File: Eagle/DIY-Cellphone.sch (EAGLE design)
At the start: 67 parts, among them IC1 MEGA1284, J1 ISP, U1 MCP73831, X1 BU-SMA-V, X3 CCM03-3002 R102

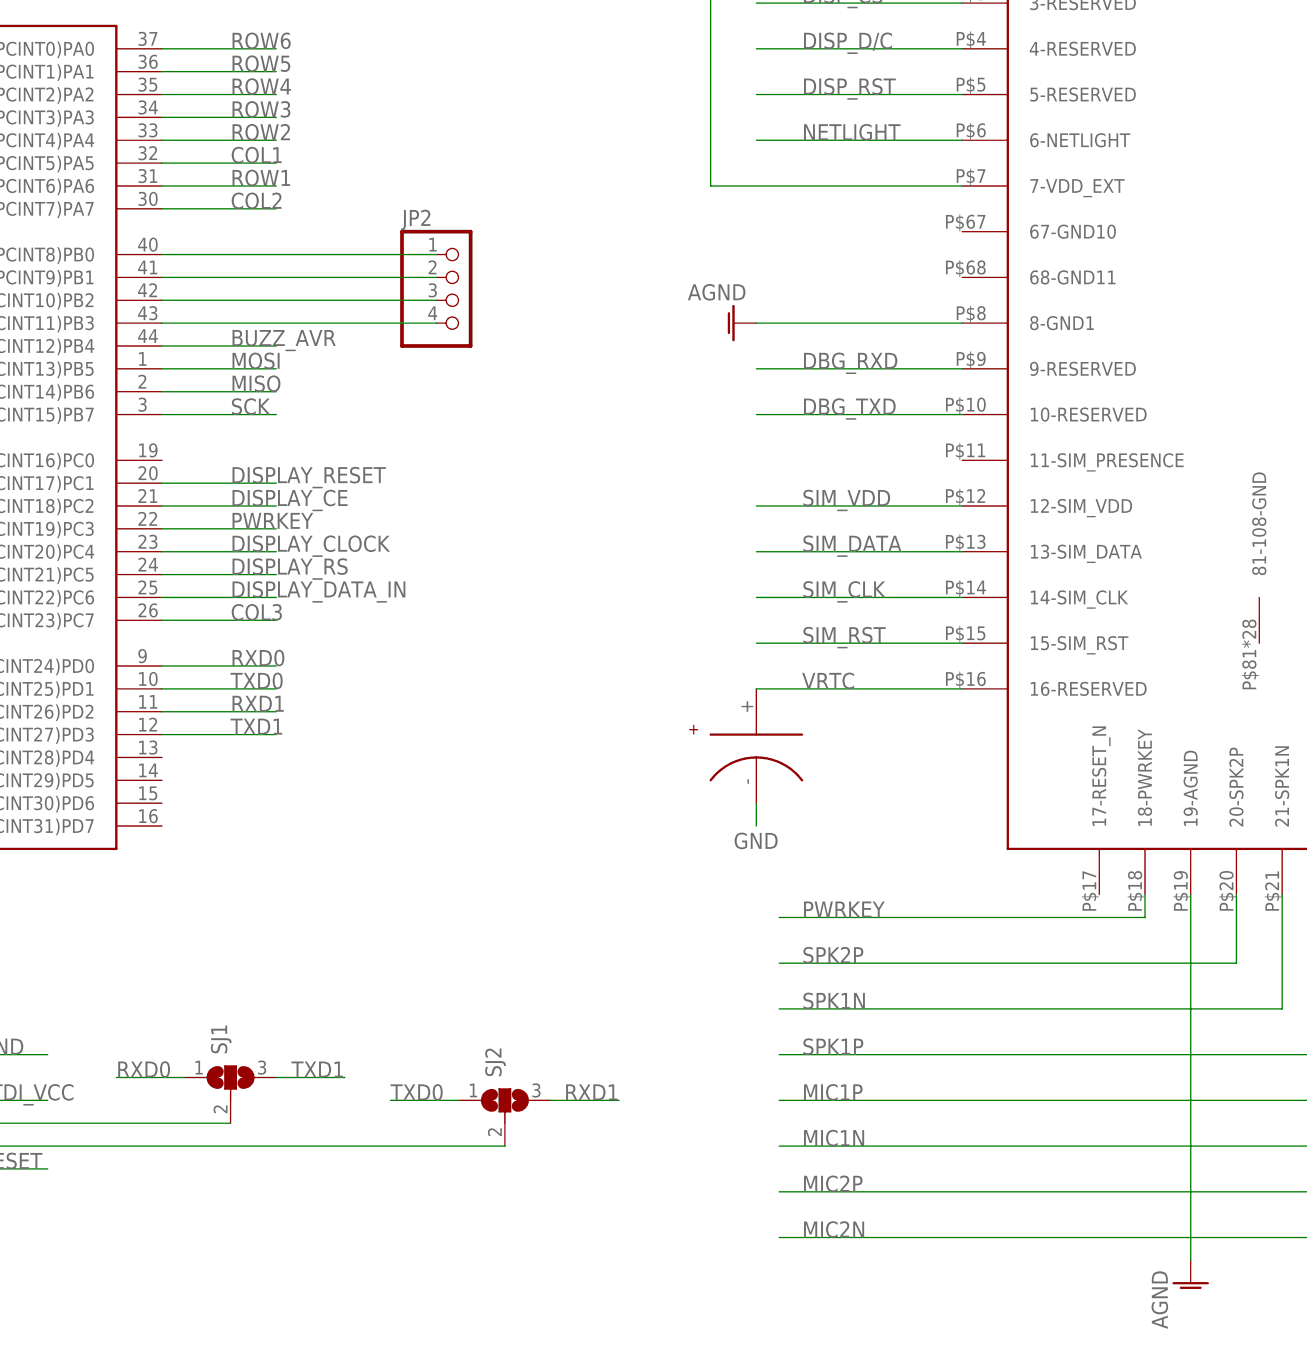
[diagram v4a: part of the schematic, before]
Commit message: Add transistors and finish routing.
PWRKEY and RESET_N now have transistors between UC15 module and
ATmega1284.
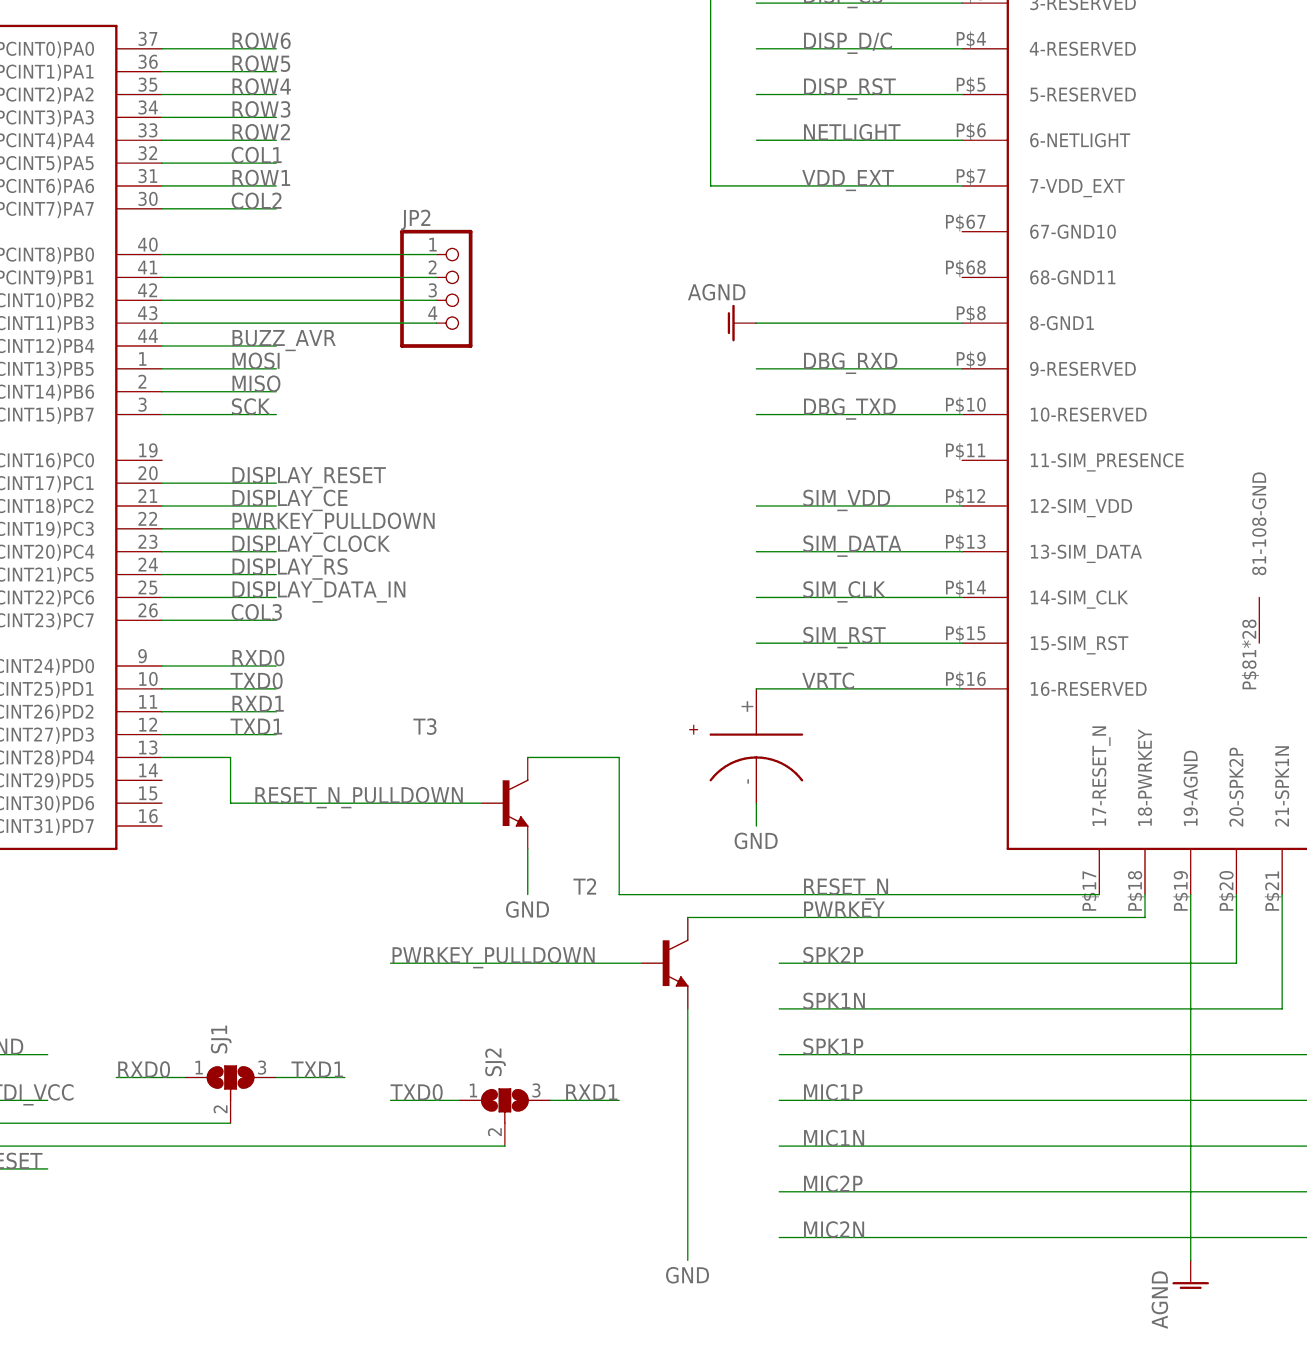
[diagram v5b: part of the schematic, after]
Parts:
- added T2, T3: (no value), transistor:MMBT3904LT1-NPN-SOT23-BEC
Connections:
- net N$2 renamed VDD_EXT
- new net PWRKEY_PULLDOWN: IC1.(TMS/PCINT19)PC3, T2.B
- new net RESET_N: T3.C, U$6.17-RESET_N
- new net RESET_N_PULLDOWN: IC1.(XCK1/OC1B/PCINT28)PD4, T3.B
- net GND: now also T2.E, T3.E
- net PWRKEY: now also T2.C; no longer IC1.(TMS/PCINT19)PC3
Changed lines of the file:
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@@
 <?xml version="1.0" encoding="utf-8"?>
 <!DOCTYPE eagle SYSTEM "eagle.dtd">
-<eagle version="6.6.0">
+<eagle version="7.1.0">
 <drawing>
 <settings>
@@
 <part name="U$6" library="cellphone" deviceset="UC15" device=""/>
 <part name="U2" library="SparkFun-DigitalIC" deviceset="TXB0104PWR" device="SOIC14"/>
+<part name="T2" library="transistor" deviceset="*-NPN-" device="SOT23-BEC" technology="MMBT3904LT1"/>
+<part name="T3" library="transistor" deviceset="*-NPN-" device="SOT23-BEC" technology="MMBT3904LT1"/>
 </parts>
 <sheets>
@@
 <instance part="U$6" gate="G$1" x="147.32" y="91.44"/>
 <instance part="U2" gate="G$1" x="76.2" y="172.72" rot="R180"/>
+<instance part="T2" gate="G$1" x="60.96" y="7.62"/>
+<instance part="T3" gate="G$1" x="43.18" y="25.4"/>
 </instances>
 <busses>
@@
 <label x="73.66" y="200.66" size="1.778" layer="95"/>
 </segment>
+<segment>
+<pinref part="T2" gate="G$1" pin="E"/>
+<wire x1="63.5" y1="2.54" x2="63.5" y2="-25.4" width="0.1524" layer="91"/>
+<label x="60.96" y="-27.94" size="1.778" layer="95"/>
+</segment>
+<segment>
+<pinref part="T3" gate="G$1" pin="E"/>
+<wire x1="45.72" y1="20.32" x2="45.72" y2="15.24" width="0.1524" layer="91"/>
+<label x="43.18" y="12.7" size="1.778" layer="95"/>
+</segment>
 </net>
 <net name="DISP_DATA" class="0">
@@
 <segment>
 <wire x1="114.3" y1="15.24" x2="114.3" y2="12.7" width="0.1524" layer="91"/>
-<wire x1="114.3" y1="12.7" x2="73.66" y2="12.7" width="0.1524" layer="91"/>
+<wire x1="114.3" y1="12.7" x2="63.5" y2="12.7" width="0.1524" layer="91"/>
 <label x="76.2" y="12.7" size="1.778" layer="95"/>
 <pinref part="U$6" gate="G$1" pin="18-PWRKEY"/>
-</segment>
-<segment>
-<pinref part="IC1" gate="G$1" pin="(TMS/PCINT19)PC3"/>
-<wire x1="5.08" y1="55.88" x2="17.78" y2="55.88" width="0.1524" layer="91"/>
-<label x="12.7" y="55.88" size="1.778" layer="95"/>
+<pinref part="T2" gate="G$1" pin="C"/>
 </segment>
 </net>
@@
 </segment>
 </net>
-<net name="N$2" class="0">
+<net name="VDD_EXT" class="0">
 <segment>
 <pinref part="U$6" gate="G$1" pin="7-VDD_EXT"/>
@@
 <wire x1="91.44" y1="139.7" x2="78.74" y2="139.7" width="0.1524" layer="91"/>
 <junction x="78.74" y="139.7"/>
-</segment>
-</net>
+<label x="76.2" y="93.98" size="1.778" layer="95"/>
+</segment>
+</net>
+<net name="PWRKEY_PULLDOWN" class="0">
+<segment>
+<pinref part="IC1" gate="G$1" pin="(TMS/PCINT19)PC3"/>
+<wire x1="5.08" y1="55.88" x2="17.78" y2="55.88" width="0.1524" layer="91"/>
+<label x="12.7" y="55.88" size="1.778" layer="95"/>
+</segment>
+<segment>
+<pinref part="T2" gate="G$1" pin="B"/>
+<wire x1="58.42" y1="7.62" x2="30.48" y2="7.62" width="0.1524" layer="91"/>
+<label x="30.48" y="7.62" size="1.778" layer="95"/>
+</segment>
+</net>
+<net name="RESET_N" class="0">
+<segment>
+<pinref part="U$6" gate="G$1" pin="17-RESET_N"/>
+<wire x1="109.22" y1="15.24" x2="55.88" y2="15.24" width="0.1524" layer="91"/>
+<wire x1="55.88" y1="15.24" x2="55.88" y2="30.48" width="0.1524" layer="91"/>
+<pinref part="T3" gate="G$1" pin="C"/>
+<wire x1="55.88" y1="30.48" x2="45.72" y2="30.48" width="0.1524" layer="91"/>
+<label x="76.2" y="15.24" size="1.778" layer="95"/>
+</segment>
+</net>
+<net name="RESET_N_PULLDOWN" class="0">
+<segment>
+<pinref part="T3" gate="G$1" pin="B"/>
+<wire x1="40.64" y1="25.4" x2="12.7" y2="25.4" width="0.1524" layer="91"/>
+<label x="15.24" y="25.4" size="1.778" layer="95"/>
+<wire x1="12.7" y1="25.4" x2="12.7" y2="30.48" width="0.1524" layer="91"/>
+<pinref part="IC1" gate="G$1" pin="(XCK1/OC1B/PCINT28)PD4"/>
+<wire x1="12.7" y1="30.48" x2="5.08" y2="30.48" width="0.1524" layer="91"/>
+</segment>
+</net>

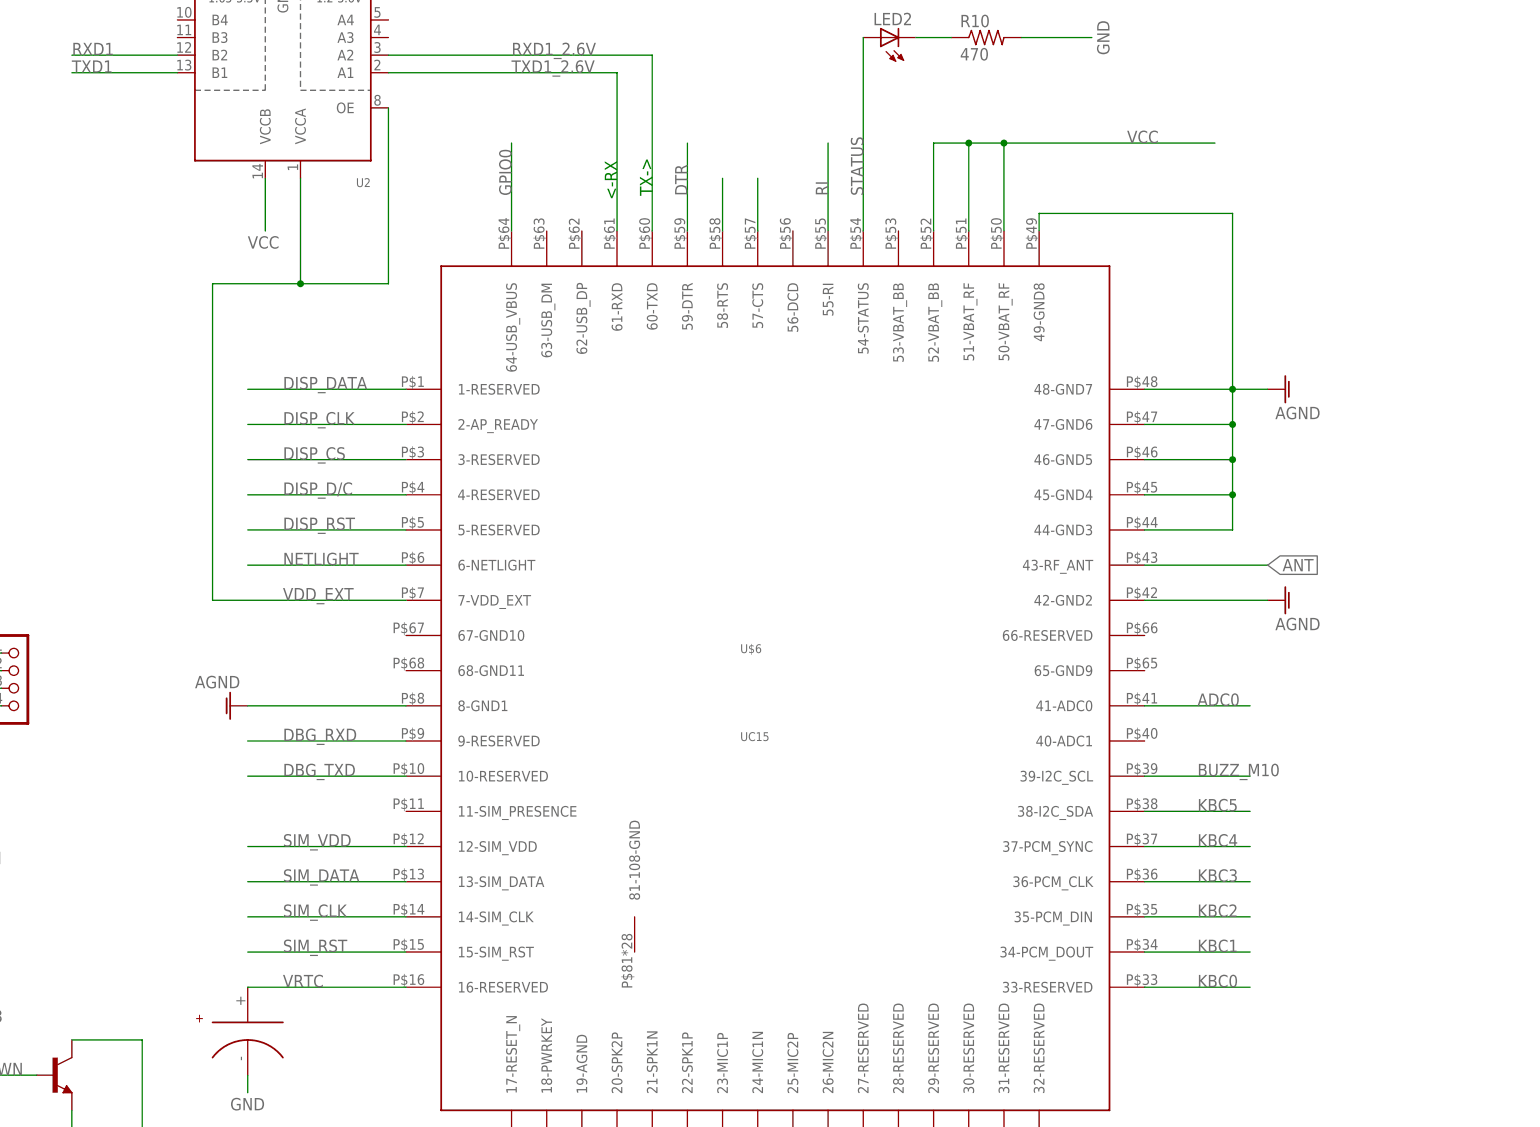
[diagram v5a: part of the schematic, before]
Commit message: Connect fourth VCC pin and additional GND pins.
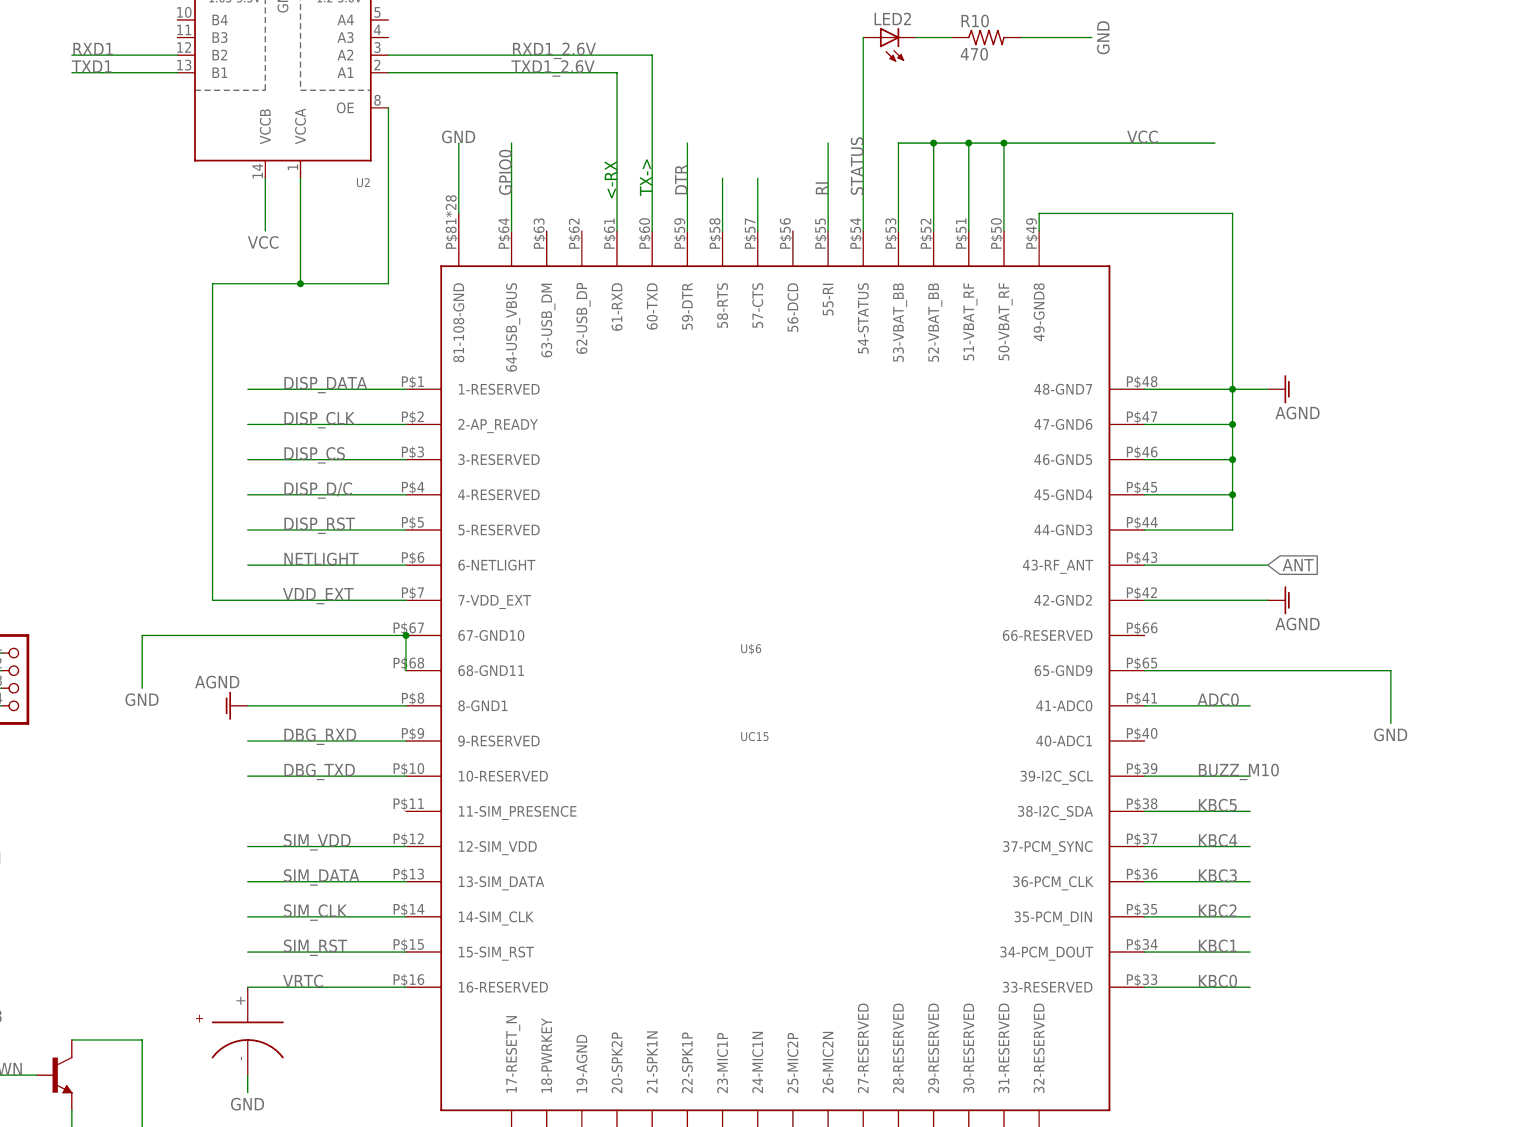
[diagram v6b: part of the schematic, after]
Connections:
- net GND: now also U$6.65-GND9, U$6.67-GND10, U$6.68-GND11, U$6.81-108-GND
- net VCC: now also U$6.53-VBAT_BB
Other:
- moved on the sheet: U$6
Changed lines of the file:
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@@
 <pinref part="U$6" gate="G$1" pin="51-VBAT_RF"/>
 <pinref part="U$6" gate="G$1" pin="52-VBAT_BB"/>
+<pinref part="U$6" gate="G$1" pin="53-VBAT_BB"/>
+<wire x1="170.18" y1="160.02" x2="165.1" y2="160.02" width="0.1524" layer="91"/>
+<wire x1="165.1" y1="160.02" x2="165.1" y2="147.32" width="0.1524" layer="91"/>
+<junction x="170.18" y="160.02"/>
 </segment>
 <segment>
@@
 <label x="43.18" y="12.7" size="1.778" layer="95"/>
 </segment>
+<segment>
+<pinref part="U$6" gate="G$1" pin="67-GND10"/>
+<pinref part="U$6" gate="G$1" pin="68-GND11"/>
+<wire x1="93.98" y1="88.9" x2="93.98" y2="83.82" width="0.1524" layer="91"/>
+<wire x1="93.98" y1="88.9" x2="55.88" y2="88.9" width="0.1524" layer="91"/>
+<wire x1="55.88" y1="88.9" x2="55.88" y2="81.28" width="0.1524" layer="91"/>
+<junction x="93.98" y="88.9"/>
+<label x="53.34" y="78.74" size="1.778" layer="95"/>
+</segment>
+<segment>
+<pinref part="U$6" gate="G$1" pin="65-GND9"/>
+<wire x1="200.66" y1="83.82" x2="236.22" y2="83.82" width="0.1524" layer="91"/>
+<wire x1="236.22" y1="83.82" x2="236.22" y2="76.2" width="0.1524" layer="91"/>
+<label x="233.68" y="73.66" size="1.778" layer="95"/>
+</segment>
+<segment>
+<pinref part="U$6" gate="G$1" pin="81-108-GND"/>
+<wire x1="101.6" y1="149.86" x2="101.6" y2="160.02" width="0.1524" layer="91"/>
+<label x="99.06" y="160.02" size="1.778" layer="95"/>
+</segment>
 </net>
